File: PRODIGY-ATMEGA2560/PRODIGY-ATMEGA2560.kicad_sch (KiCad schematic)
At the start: 3 parts, among them J1 Bus_M.2_Socket_B, U2 CH340G

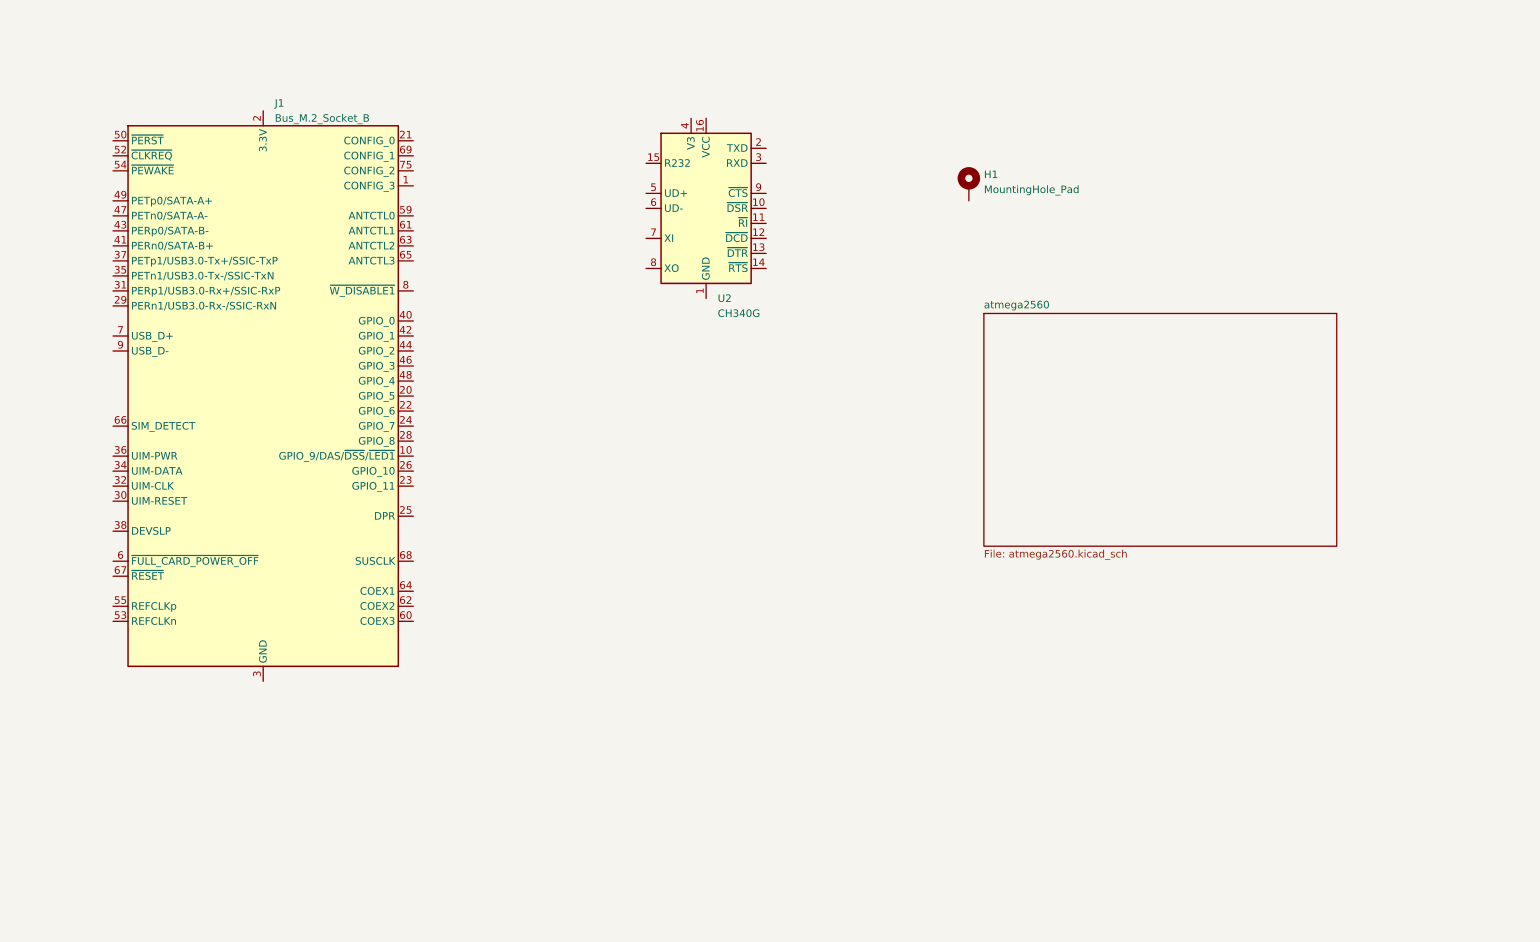
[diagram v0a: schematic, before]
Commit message: ATMEGA2560 schematic finished
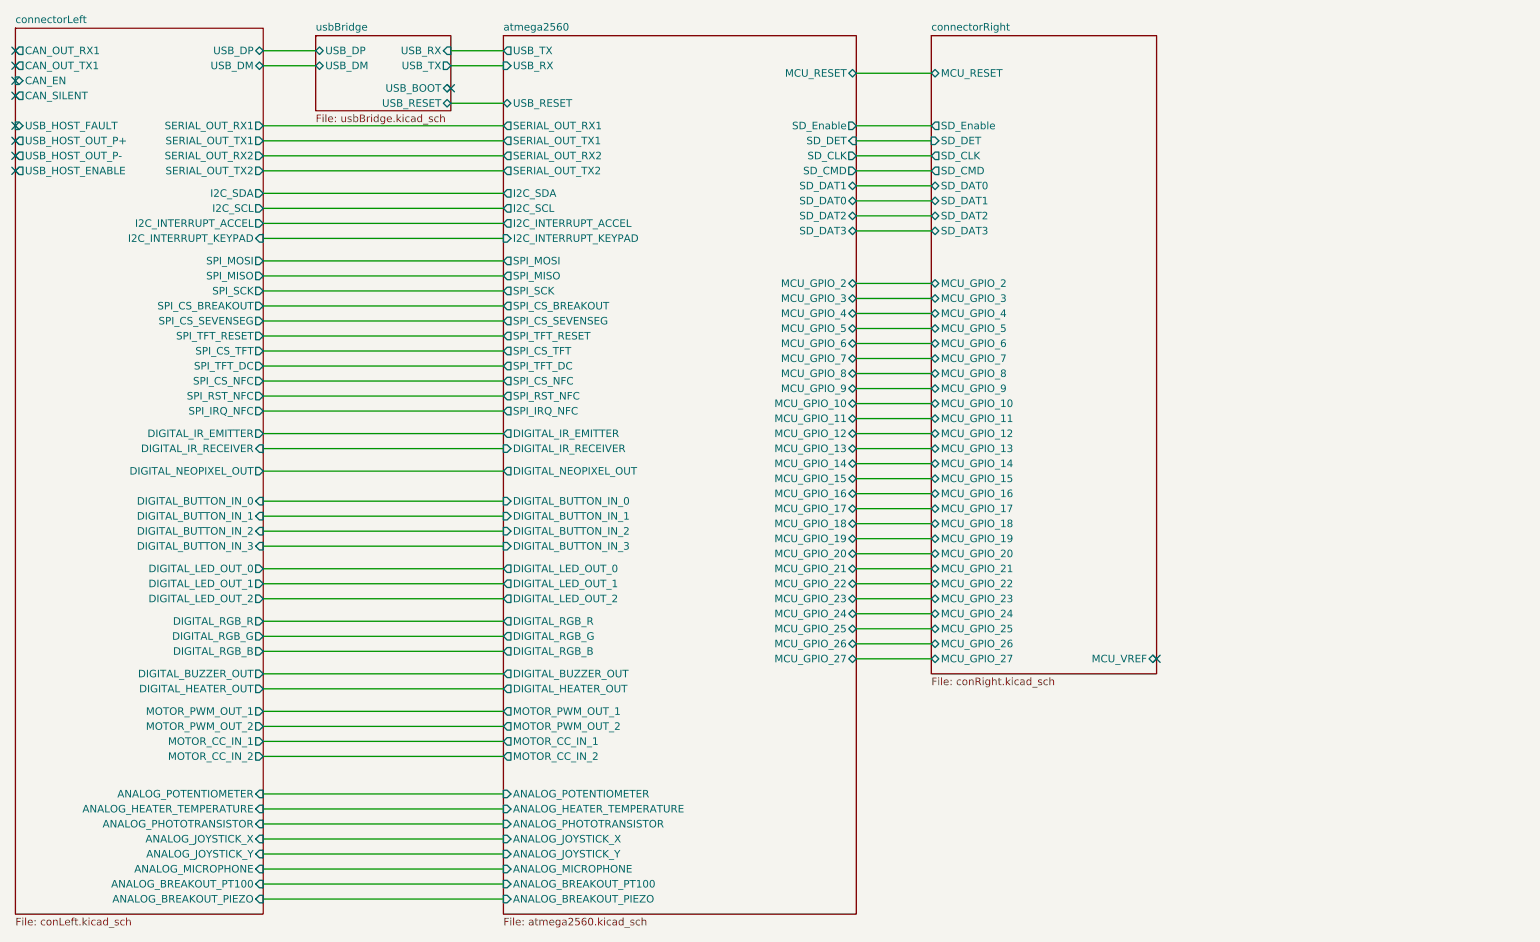
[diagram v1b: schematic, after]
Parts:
- removed H1: MountingHole_Pad, Library:m.2_mounting_hole, symbol Mechanical:MountingHole_Pad
- removed J1: Bus_M.2_Socket_B, NGFF:NGFF_B, symbol Connector:Bus_M.2_Socket_B
- removed U2: CH340G, Package_SO:SOIC-16_3.9x9.9mm_P1.27mm, symbol Interface_USB:CH340G
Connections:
- no-connect marks 0 -> 10
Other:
- added sheet connectorLeft (conLeft.kicad_sch)
- added sheet connectorRight (conRight.kicad_sch)
- added sheet usbBridge (usbBridge.kicad_sch)
- sheet atmega2560 ports: added ANALOG_BREAKOUT_PIEZO, ANALOG_BREAKOUT_PT100, ANALOG_HEATER_TEMPERATURE, ANALOG_JOYSTICK_X, ANALOG_JOYSTICK_Y, ANALOG_MICROPHONE, ANALOG_PHOTOTRANSISTOR, ANALOG_POTENTIOMETER, DIGITAL_BUTTON_IN_0, DIGITAL_BUTTON_IN_1, DIGITAL_BUTTON_IN_2, DIGITAL_BUTTON_IN_3, DIGITAL_BUZZER_OUT, DIGITAL_HEATER_OUT, DIGITAL_IR_EMITTER, DIGITAL_IR_RECEIVER, DIGITAL_LED_OUT_0, DIGITAL_LED_OUT_1, DIGITAL_LED_OUT_2, DIGITAL_NEOPIXEL_OUT, DIGITAL_RGB_B, DIGITAL_RGB_G, DIGITAL_RGB_R, I2C_INTERRUPT_ACCEL, I2C_INTERRUPT_KEYPAD, I2C_SCL, I2C_SDA, MCU_GPIO_10, MCU_GPIO_11, MCU_GPIO_12, MCU_GPIO_13, MCU_GPIO_14, MCU_GPIO_15, MCU_GPIO_16, MCU_GPIO_17, MCU_GPIO_18, MCU_GPIO_19, MCU_GPIO_2, MCU_GPIO_20, MCU_GPIO_21, MCU_GPIO_22, MCU_GPIO_23, MCU_GPIO_24, MCU_GPIO_25, MCU_GPIO_26, MCU_GPIO_27, MCU_GPIO_3, MCU_GPIO_4, MCU_GPIO_5, MCU_GPIO_6, MCU_GPIO_7, MCU_GPIO_8, MCU_GPIO_9, MCU_RESET, MOTOR_CC_IN_1, MOTOR_CC_IN_2, MOTOR_PWM_OUT_1, MOTOR_PWM_OUT_2, SD_CLK, SD_CMD, SD_DAT0, SD_DAT1, SD_DAT2, SD_DAT3, SD_DET, SD_Enable, SERIAL_OUT_RX1, SERIAL_OUT_RX2, SERIAL_OUT_TX1, SERIAL_OUT_TX2, SPI_CS_BREAKOUT, SPI_CS_NFC, SPI_CS_SEVENSEG, SPI_CS_TFT, SPI_IRQ_NFC, SPI_MISO, SPI_MOSI, SPI_RST_NFC, SPI_SCK, SPI_TFT_DC, SPI_TFT_RESET, USB_RESET, USB_RX, USB_TX; removed none

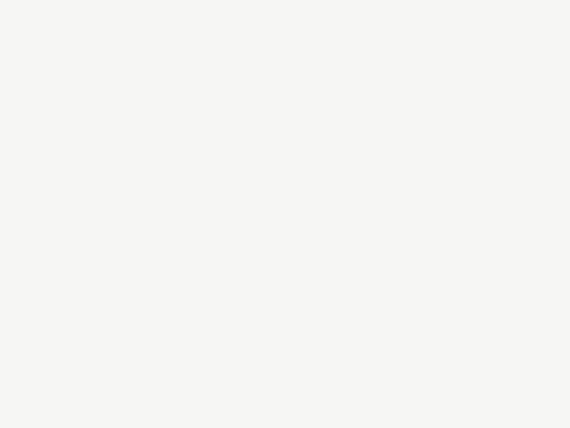
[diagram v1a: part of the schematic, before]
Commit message: All footprint assosiations have been made across all schematics.
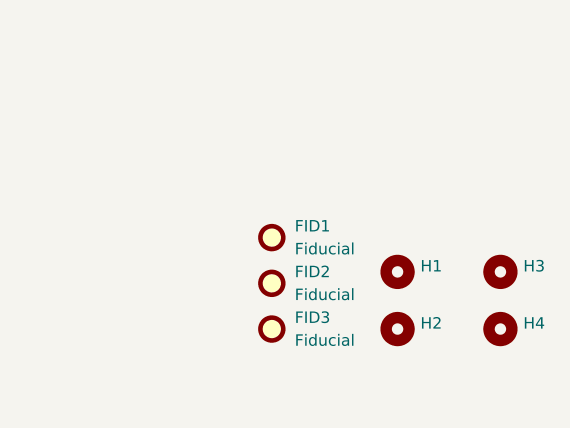
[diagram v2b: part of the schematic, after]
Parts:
- added FID1, FID2, FID3: Fiducial, Fiducial:Fiducial_1mm_Mask3mm, symbol Mechanical:Fiducial
- added H1, H2, H3, H4: MountingHole, MountingHole:MountingHole_3.2mm_M3_ISO7380_Pad_TopBottom, symbol Mechanical:MountingHole

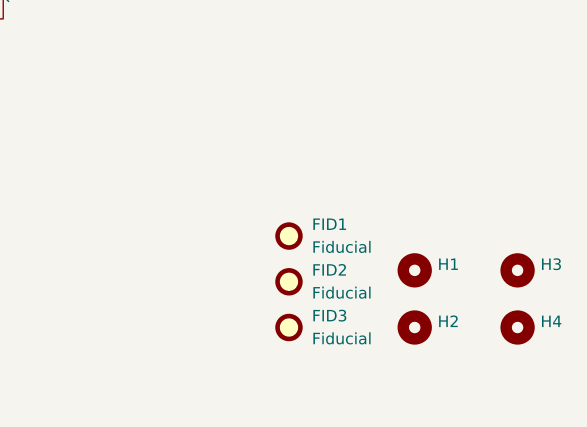
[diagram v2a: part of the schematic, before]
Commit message: ESP32 and ATMEGA bom done.
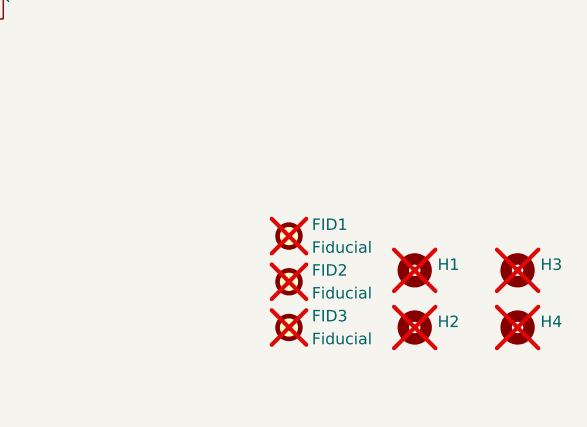
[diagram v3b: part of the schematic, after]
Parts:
- FID1, FID2, FID3, H1, H2, H3, H4: now not fitted
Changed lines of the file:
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@@
 		(in_bom yes)
 		(on_board yes)
-		(dnp no)
+		(dnp yes)
 		(fields_autoplaced yes)
 		(property "Reference" "H2"
@@
 		(in_bom yes)
 		(on_board yes)
-		(dnp no)
+		(dnp yes)
 		(fields_autoplaced yes)
 		(property "Reference" "H4"
@@
 		(in_bom yes)
 		(on_board yes)
-		(dnp no)
+		(dnp yes)
 		(fields_autoplaced yes)
 		(property "Reference" "FID3"
@@
 		(in_bom yes)
 		(on_board yes)
-		(dnp no)
+		(dnp yes)
 		(fields_autoplaced yes)
 		(property "Reference" "FID1"
@@
 		(in_bom yes)
 		(on_board yes)
-		(dnp no)
+		(dnp yes)
 		(fields_autoplaced yes)
 		(property "Reference" "H3"
@@
 		(in_bom yes)
 		(on_board yes)
-		(dnp no)
+		(dnp yes)
 		(fields_autoplaced yes)
 		(property "Reference" "H1"
@@
 		(in_bom yes)
 		(on_board yes)
-		(dnp no)
+		(dnp yes)
 		(fields_autoplaced yes)
 		(property "Reference" "FID2"

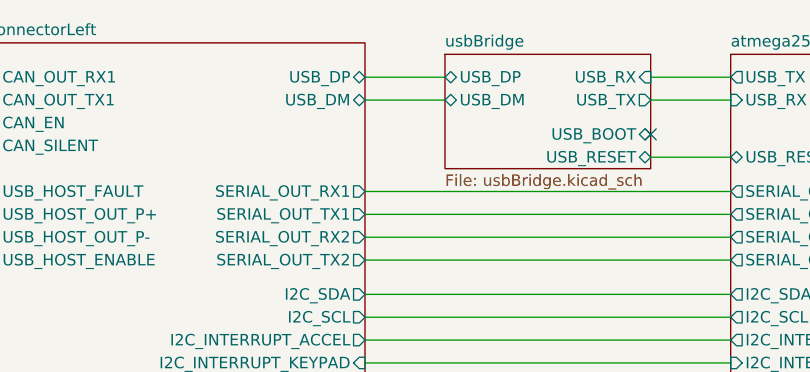
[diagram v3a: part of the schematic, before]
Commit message: Atmega layout done. orientation and alignment testing done. routing started.
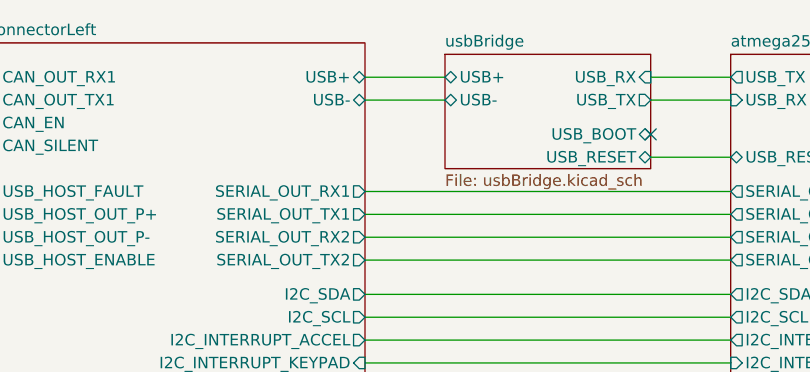
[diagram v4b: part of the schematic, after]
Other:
- sheet connectorLeft ports: added USB+, USB-; removed USB_DM, USB_DP
- sheet usbBridge ports: added USB+, USB-; removed USB_DM, USB_DP
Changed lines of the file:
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@@
-			)
-		)
-		(pin "USB_DP" bidirectional
-			(at 67.31 21.59 0)
-			(effects
-				(font
-					(size 1.27 1.27)
-				)
-				(justify right)
 			)
 		)
@@
 			)
 		)
-		(pin "USB_DM" bidirectional
-			(at 67.31 24.13 0)
-			(effects
-				(font
-					(size 1.27 1.27)
-				)
-				(justify right)
-			)
-		)
 		(pin "CAN_OUT_RX1" output
 			(at 25.4 21.59 180)
@@
 				)
 				(justify left)
+			)
+		)
+		(pin "USB-" bidirectional
+			(at 67.31 24.13 0)
+			(effects
+				(font
+					(size 1.27 1.27)
+				)
+				(justify right)
+			)
+		)
+		(pin "USB+" bidirectional
+			(at 67.31 21.59 0)
+			(effects
+				(font
+					(size 1.27 1.27)
+				)
+				(justify right)
 			)
 		)
@@
 			)
 		)
-		(pin "USB_DM" bidirectional
-			(at 76.2 24.13 180)
-			(effects
-				(font
-					(size 1.27 1.27)
-				)
-				(justify left)
-			)
-		)
-		(pin "USB_DP" bidirectional
-			(at 76.2 21.59 180)
-			(effects
-				(font
-					(size 1.27 1.27)
-				)
-				(justify left)
-			)
-		)
 		(pin "USB_BOOT" bidirectional
 			(at 99.06 27.94 0)
@@
 			)
 		)
+		(pin "USB-" bidirectional
+			(at 76.2 24.13 180)
+			(effects
+				(font
+					(size 1.27 1.27)
+				)
+				(justify left)
+			)
+		)
+		(pin "USB+" bidirectional
+			(at 76.2 21.59 180)
+			(effects
+				(font
+					(size 1.27 1.27)
+				)
+				(justify left)
+			)
+		)
